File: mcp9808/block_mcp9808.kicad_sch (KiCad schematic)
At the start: 21 parts, among them Q1 AO3400A, Q2 AO3400A, Q3 AO3400A, U1 MCP9808_MSOP

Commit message: [Rushil] added user drwaing for block outline, removed test point, reduced the size of block and solved white space issue
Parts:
- removed TP1: TestPoint, TestPoint:TestPoint_Pad_D2.5mm, symbol Library:TestPoint
- C1: LCSC part C22399626 -> (none); LCSC_part# (none) -> C22399626
- C2: LCSC part# C14663 -> (none); LCSC_part# (none) -> C14663
- Q1: Check_prices https://www.snapeda.com/parts/AO3400A/Alpha/view-part/?ref=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 -> (none); LCSC part# C347475 -> (none); LCSC_part# (none) -> C347475; MANUFACTURER Alpha & Omega Semiconductor -> (none); MAXIMUM_PACKAGE_HEIGHT 1.25 mm -> (none); MF Alpha & Omega Semiconductor -> (none); MP AO3400A -> (none); PARTREV L -> (none); STANDARD IPC 7351B -> (none); SnapEDA_Link https://www.snapeda.com/parts/AO3400A/Alpha/view-part/?ref=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 -> (none)
- Q2, Q3: Check_prices https://www.snapeda.com/parts/AO3400A/Alpha/view-part/?ref=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 -> (none); LCSC part # C347475 -> (none); LCSC_part# (none) -> C347475; MANUFACTURER Alpha & Omega Semiconductor -> (none); MAXIMUM_PACKAGE_HEIGHT 1.25 mm -> (none); MF Alpha & Omega Semiconductor -> (none); MP AO3400A -> (none); PARTREV L -> (none); STANDARD IPC 7351B -> (none); SnapEDA_Link https://www.snapeda.com/parts/AO3400A/Alpha/view-part/?ref=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 -> (none)
- R1, R2: LCSC_part# (none) -> C25804; MPN (none) -> 0603WAF1002T5E
- R10: LCSC part# C105588 -> (none); LCSC_part# (none) -> C105588; MPN (none) -> RC0603FR-07100RL; MPN  RC0603FR-07100RL -> (none)
- R11: LCSC part# C105588 -> (none); LCSC_part# (none) -> C105588
- R3: LCSC part C25804 -> (none); LCSC_part# (none) -> C25804
- R4, R5, R8: LCSC part # C25804 -> (none); LCSC_part# (none) -> C25804
- R6, R7: LCSC part# C25804 -> (none); LCSC_part# (none) -> C25804
- R9: LCSC Part # C105588 -> (none); LCSC_part# (none) -> C105588
- U1: LCSC part# C94847 -> (none); LCSC_part# (none) -> C94847
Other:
- note added: "2.7V=<VDD<=5.5V"

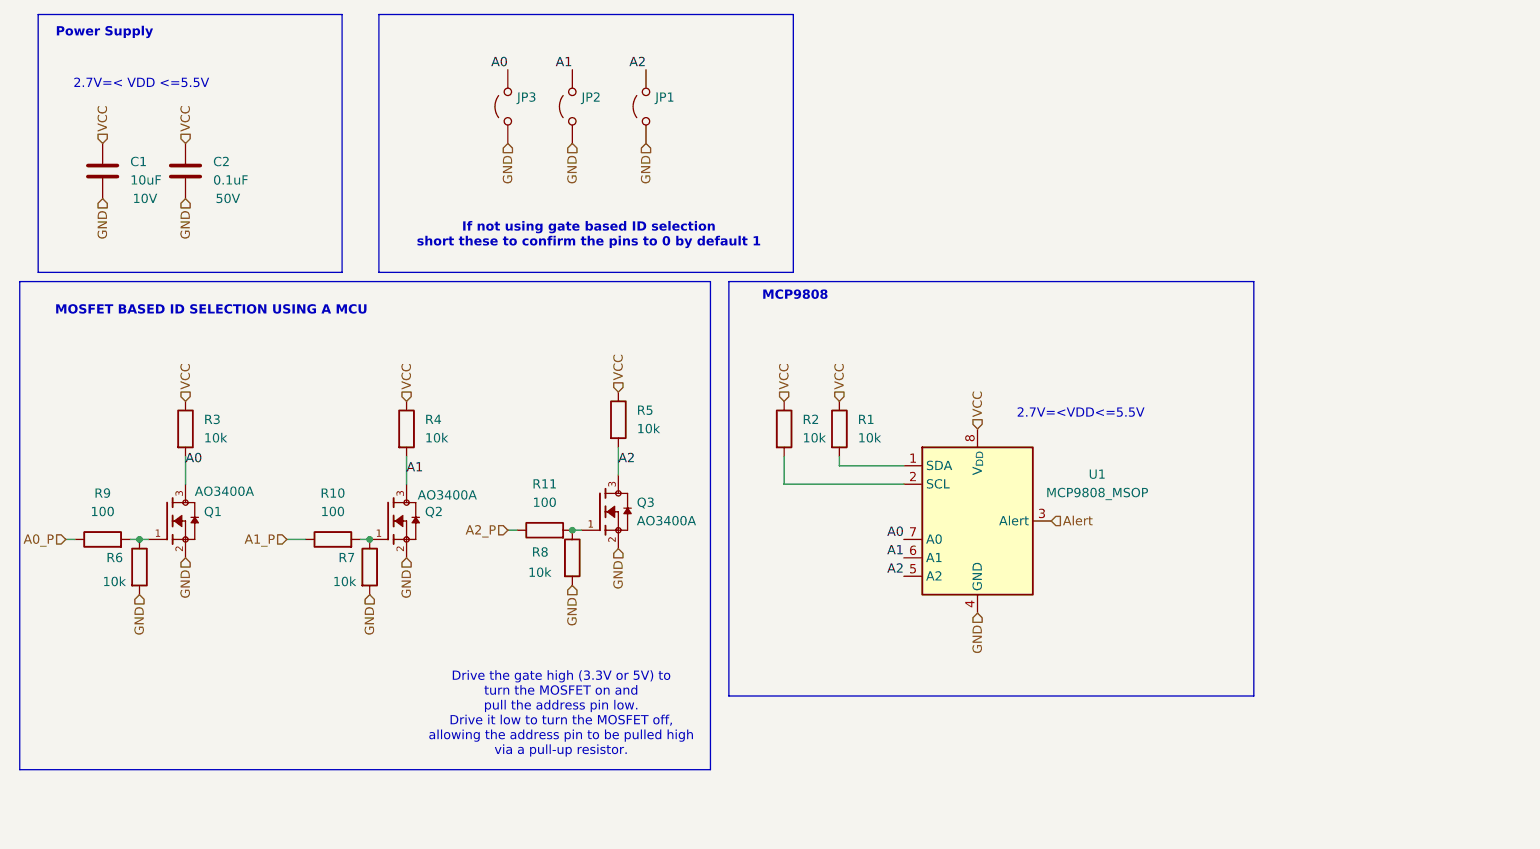
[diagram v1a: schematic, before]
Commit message: [Rushil] removed mos, made more compact, designator resize according to constraints,default id on silk screen
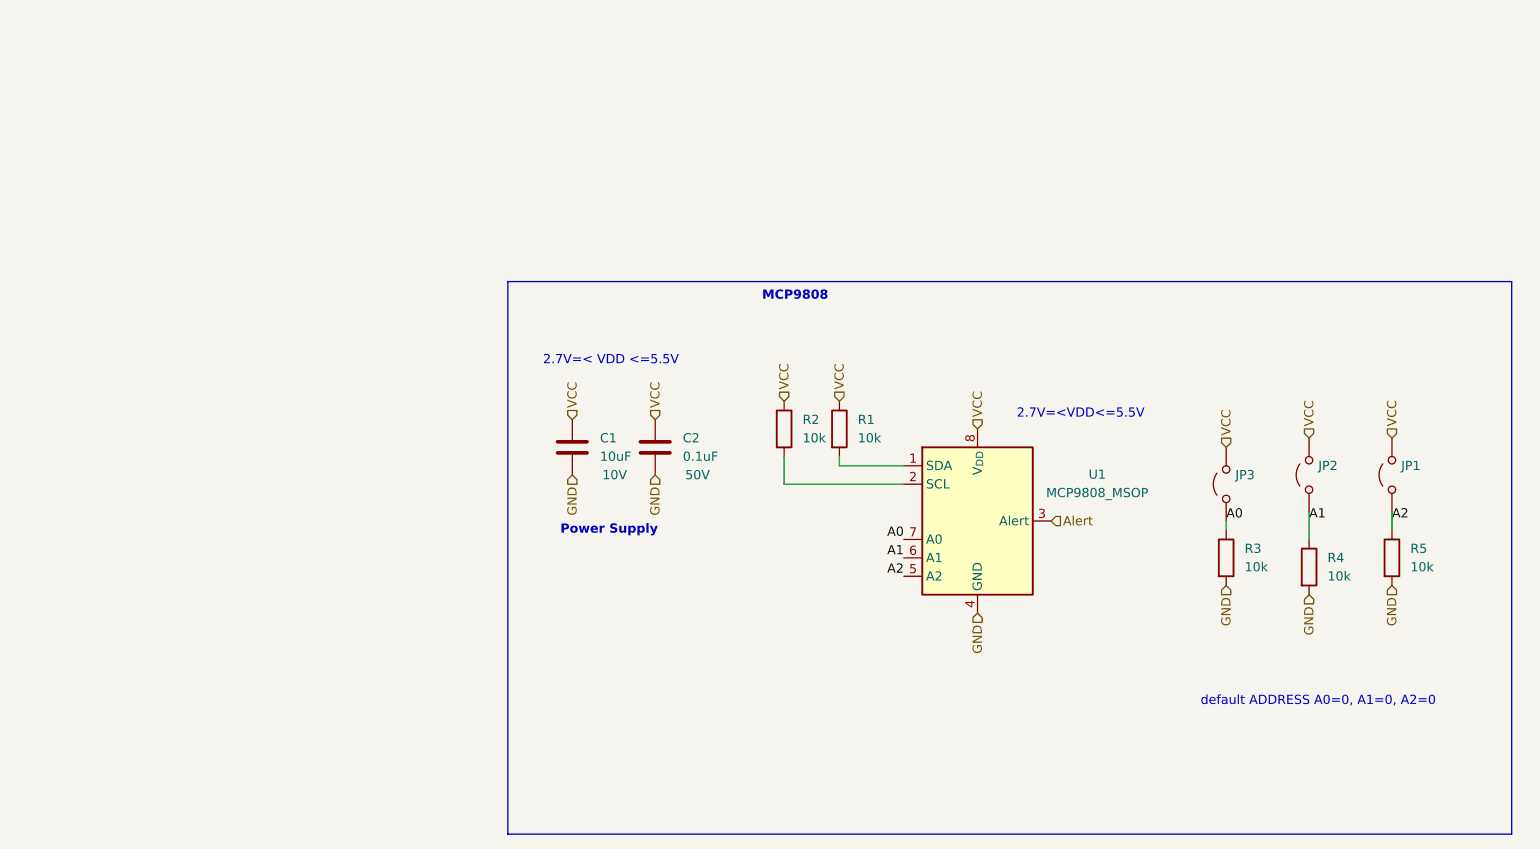
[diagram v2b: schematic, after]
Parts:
- removed Q1, Q2, Q3: AO3400A, Library:SOT95P280X125-3N, symbol Library:AO3400A
- removed R10, R11, R9: 100, Resistor_SMD:R_0603_1608Metric, symbol Library:R
- removed R6, R7, R8: 10k, Resistor_SMD:R_0603_1608Metric, symbol Library:R
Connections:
- net A0: now also JP3.1 (A), R3.1; no longer JP3.2 (B), R3.2
- net A1: now also JP2.1 (A), R4.1; no longer JP2.2 (B), R4.2
- net A2: now also JP1.1 (A), R5.1; no longer JP1.2 (B), R5.2
- net GND: now also R3.2, R4.2, R5.2; no longer JP1.1 (A), JP2.1 (A), JP3.1 (A)
- net VCC: now also JP1.2 (B), JP2.2 (B), JP3.2 (B); no longer R3.1, R4.1, R5.1
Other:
- note added: "default ADDRESS A0=0, A1=0, A2=0"
- note removed: "Drive the gate high (3.3V or 5V) to turn the MOSFET on and pull the address pin low. Drive it low to turn the MOSFET off, allowing the address pin to be pulled high via a pull-up resistor."
- note removed: "If not using gate based ID selection short these to confirm the pins to 0 by default 1"
- note removed: "MOSFET BASED ID SELECTION USING A MCU"
- moved on the sheet: C1, C2, JP1, JP2, JP3, R3, R4, R5

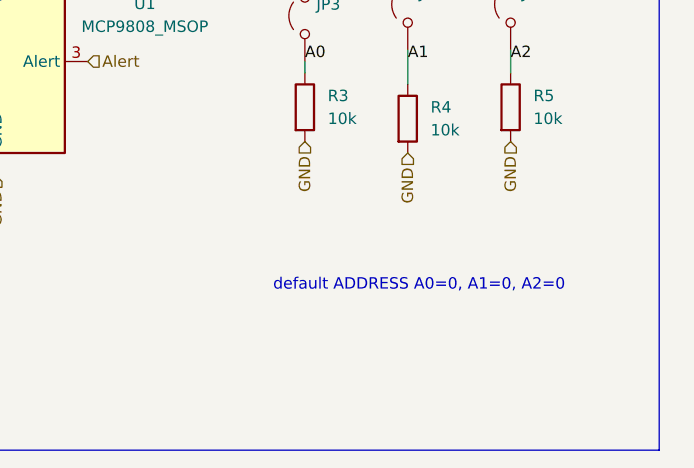
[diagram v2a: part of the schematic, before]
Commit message: [Rushil] address on silkscreen corrected and removed on pad vias
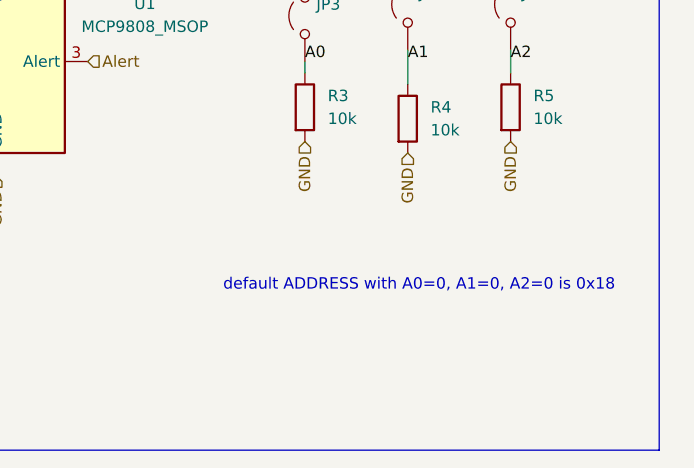
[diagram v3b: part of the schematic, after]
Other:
- note added: "default ADDRESS with A0=0, A1=0, A2=0 is 0x18"
- note removed: "default ADDRESS A0=0, A1=0, A2=0"
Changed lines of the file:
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@@
 		)
 	)
-	(text "default ADDRESS A0=0, A1=0, A2=0"
+	(text "default ADDRESS with A0=0, A1=0, A2=0 is 0x18"
 		(exclude_from_sim no)
 		(at 191.77 117.602 0)

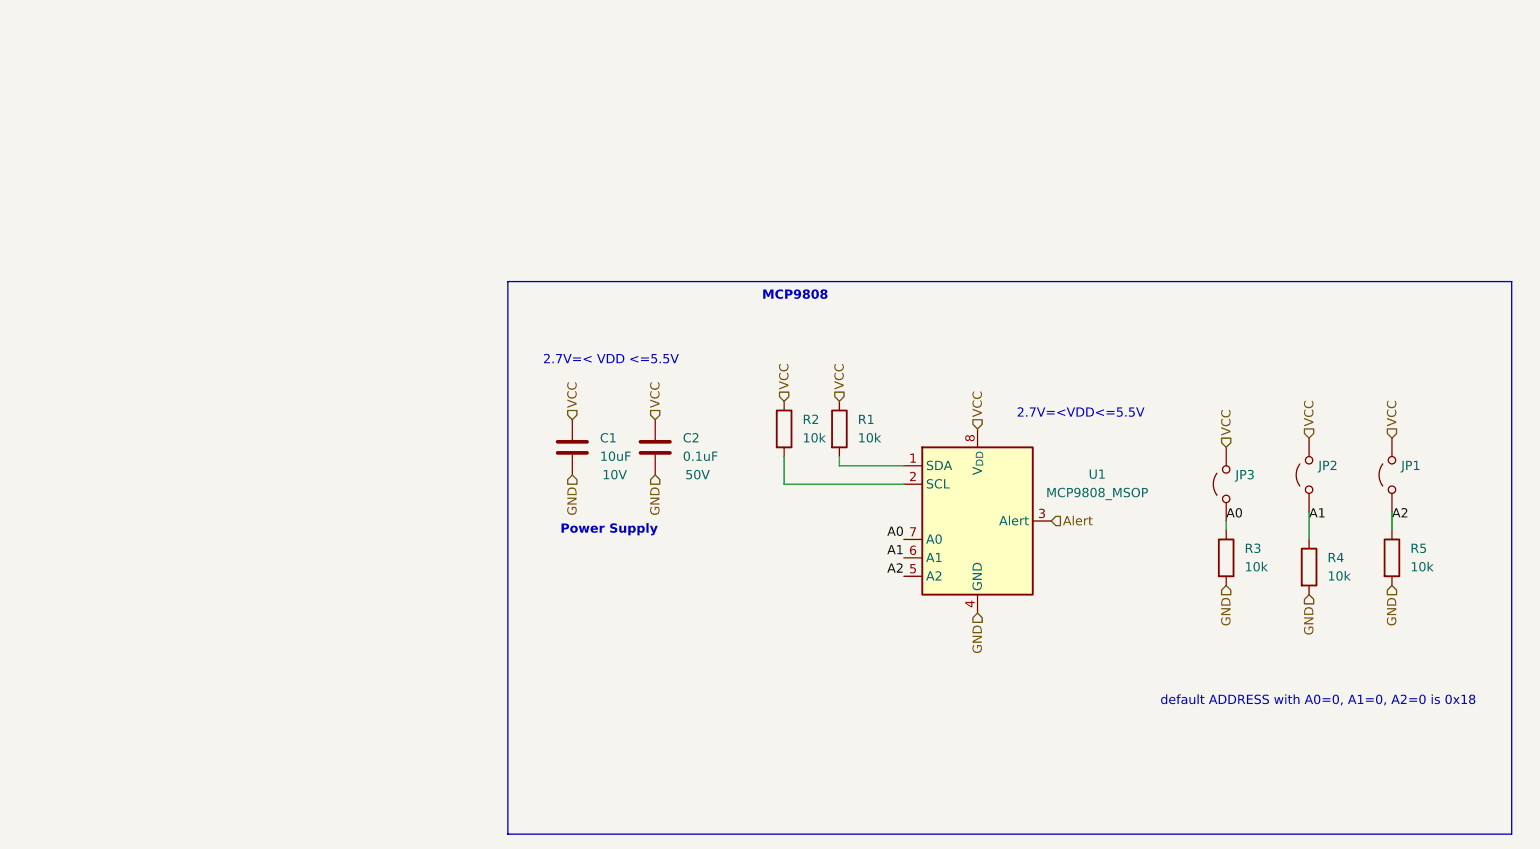
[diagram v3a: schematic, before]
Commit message: [Rushil] corrected pcb added information on both schematic and pcb user drawing correct circuit of bno055
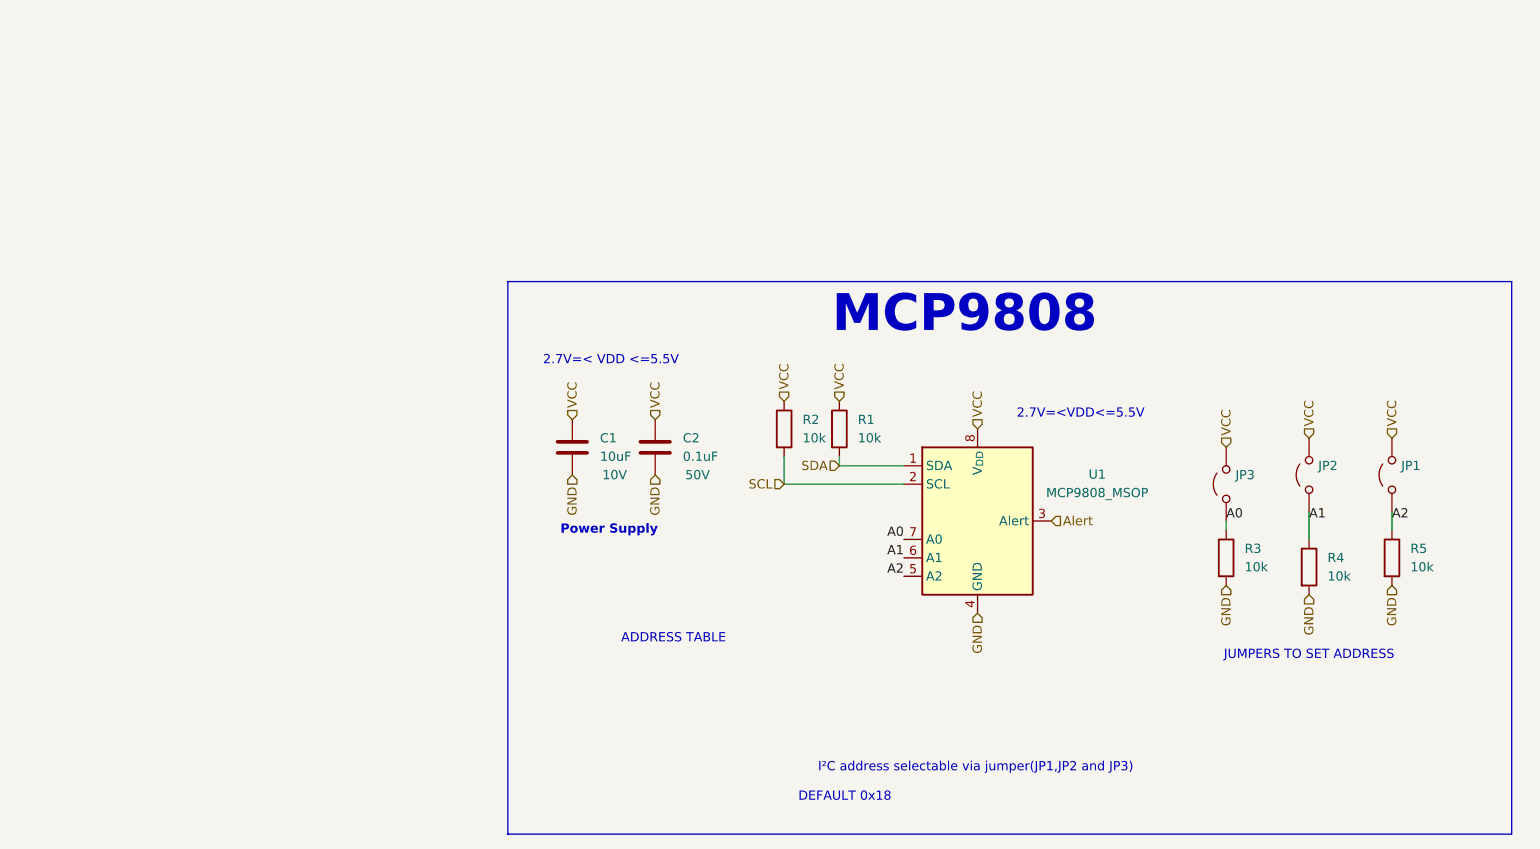
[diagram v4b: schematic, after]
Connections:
- net SDA: now reaches R1.2, U1.1 (SDA)
- net SCL: now reaches R2.2, U1.2 (SCL)
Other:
- note added: "ADDRESS TABLE"
- note added: "DEFAULT 0x18"
- note added: "I²C address selectable via jumper(JP1,JP2 and JP3)"
- note added: "JUMPERS TO SET ADDRESS"
- note removed: "default ADDRESS with A0=0, A1=0, A2=0 is 0x18"

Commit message: [Rushil] did some clean up
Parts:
- C1, C2, R1, R2, R3, R4, R5: package 0603 -> (none)
- U1: package MSOP-8 -> (none)

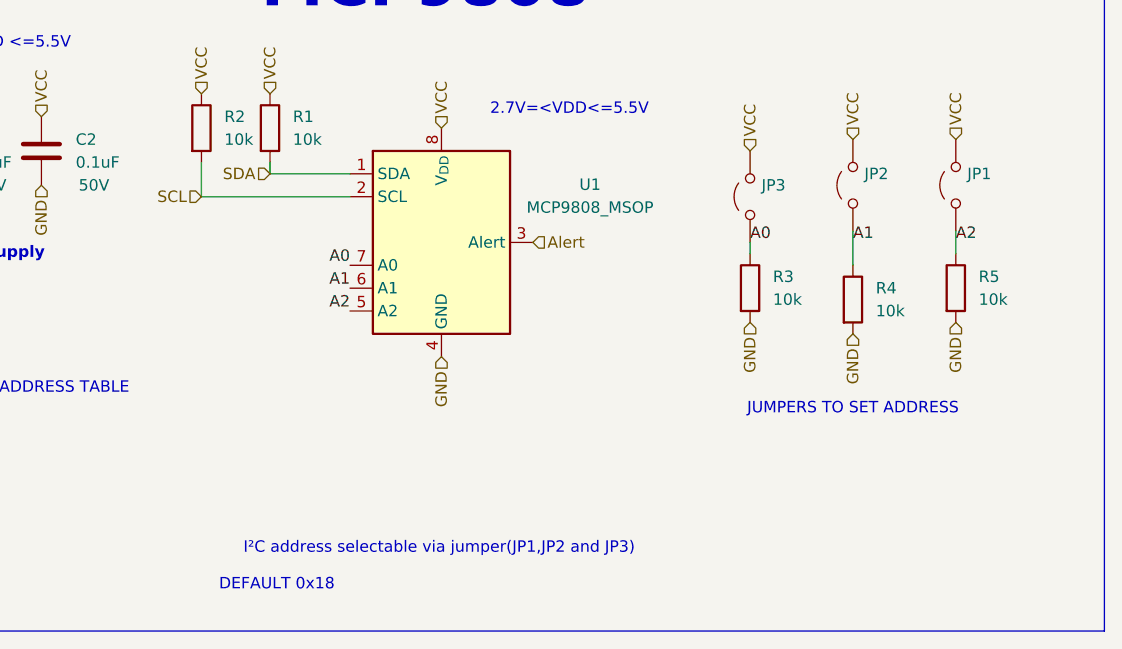
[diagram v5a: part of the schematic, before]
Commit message: Edited and finalized blocks MCP9809 and DS3231
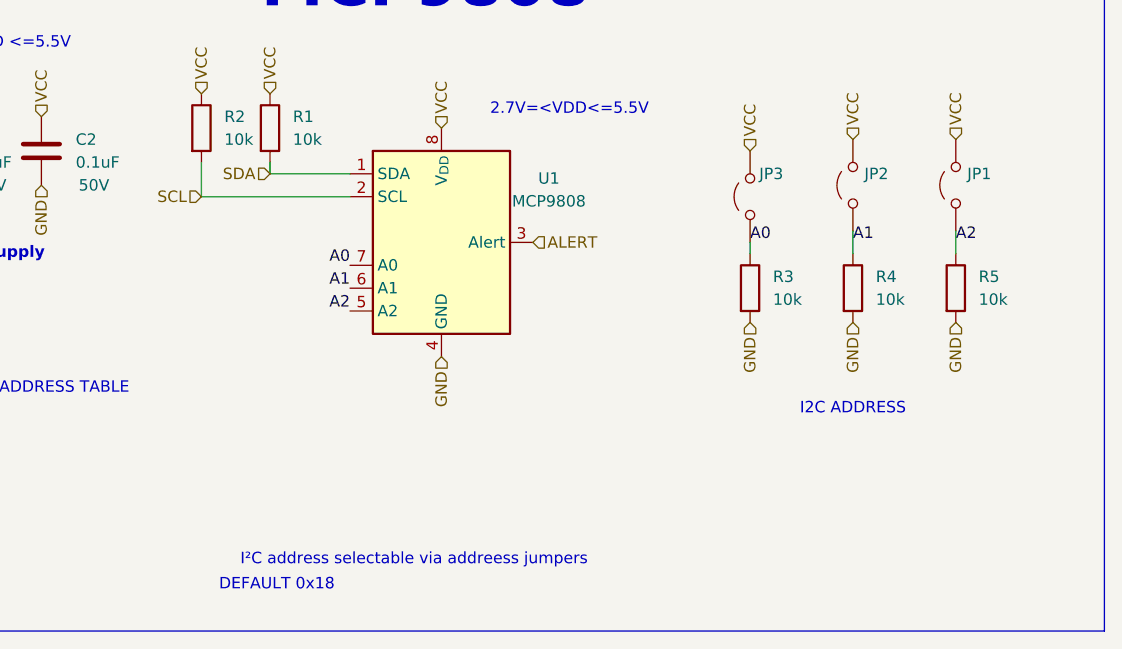
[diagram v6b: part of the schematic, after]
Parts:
- U1: value MCP9808_MSOP -> MCP9808
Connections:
- net Alert renamed ALERT
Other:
- note added: "I2C ADDRESS"
- note added: "I²C address selectable via addreess jumpers"
- note removed: "I²C address selectable via jumper(JP1,JP2 and JP3)"
- note removed: "JUMPERS TO SET ADDRESS"
- moved on the sheet: R4
